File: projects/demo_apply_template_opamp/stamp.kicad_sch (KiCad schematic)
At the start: 3 parts, among them U1 LM358

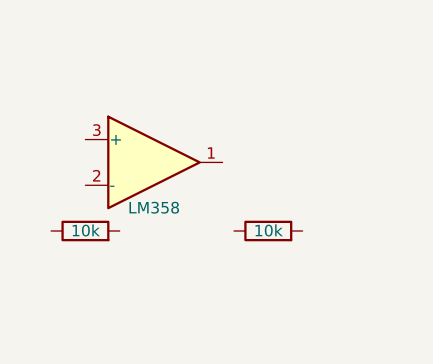
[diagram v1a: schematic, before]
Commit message: Phase 2: baked template geometry + LM358 embed fix
Templates now carry hand-authored wires/junctions/labels in relative
coords; Stamp() emits them verbatim. All 5 templates rewritten with
human conventions and self-verifying tests (gate.Check==0, TraceNets
contract, exact pin-endpoint match). flattenRawSymbol now inherits
parent properties so embedded derived symbols match KiCad 10
regeneration (fixes lib_symbol_mismatch for LM358/NE5532).

Co-Authored-By: Claude Fable 5 <noreply@anthropic.com>
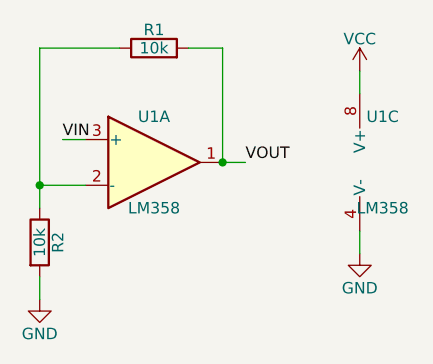
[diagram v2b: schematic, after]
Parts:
- added unit 3 of U1
- R1, R2, U1: now in the parts list
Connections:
- net at R1.1: now also R2.1, U1.2 (-)
- net VOUT: now reaches R1.2
- net VOUT: now also U1.1
- net VIN: now reaches U1.3 (+)
- net GND: now reaches R2.2
- net GND: now also U1.4 (V-)
- new net VCC: U1.8 (V+)
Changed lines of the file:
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@@
     (path "/" (page "1")))
   (symbol (lib_id "Amplifier_Operational:LM358")
-    (at 80.01 80.01 0) (unit 1) (exclude_from_sim no) (in_bom no) (on_board no) (dnp no)
+    (at 80.01 80.01 0) (unit 1) (exclude_from_sim no) (in_bom yes) (on_board yes) (dnp no)
     (property "Reference" "U1"
-      (at 80.01 80.01 0)
-      (effects
-        (font (size 1.27 1.27)) (hide yes)))
+      (at 80.01 74.93 0)
+      (effects
+        (font (size 1.27 1.27))))
     (property "Value" "LM358"
       (at 80.01 85.09 0)
@@
     (instances
       (project ""
-        (path "/e5270886-c330-482a-858b-eb20bea9dc9a" (reference "U1") (unit 1)))))
+        (path "/ca349aeb-c2b5-433f-8e31-d97ef754470a" (reference "U1") (unit 1)))))
+  (symbol (lib_id "Amplifier_Operational:LM358")
+    (at 105.41 80.01 0) (unit 3) (exclude_from_sim no) (in_bom yes) (on_board yes) (dnp no)
+    (property "Reference" "U1"
+      (at 105.41 74.93 0)
+      (effects
+        (font (size 1.27 1.27))))
+    (property "Value" "LM358"
+      (at 105.41 85.09 0)
+      (effects
+        (font (size 1.27 1.27))))
+    (property "Footprint" ""
+      (at 105.41 80.01 0)
+      (effects
+        (font (size 1.27 1.27)) (hide yes)))
+    (property "Datasheet" ""
+      (at 105.41 80.01 0)
+      (effects
+        (font (size 1.27 1.27)) (hide yes)))
+    (property "Description" ""
+      (at 105.41 80.01 0)
+      (effects
+        (font (size 1.27 1.27)) (hide yes)))
+    (pin "4")
+    (pin "8")
+    (instances
+      (project ""
+        (path "/ca349aeb-c2b5-433f-8e31-d97ef754470a" (reference "U1") (unit 3)))))
   (symbol (lib_id "Device:R")
-    (at 92.71 87.63 90) (unit 1) (exclude_from_sim no) (in_bom no) (on_board no) (dnp no)
+    (at 80.01 67.31 90) (unit 1) (exclude_from_sim no) (in_bom yes) (on_board yes) (dnp no)
     (property "Reference" "R1"
-      (at 92.71 87.63 0)
-      (effects
-        (font (size 1.27 1.27)) (hide yes)))
+      (at 80.01 65.278 90)
+      (effects
+        (font (size 1.27 1.27))))
     (property "Value" "10k"
-      (at 92.71 87.63 90)
-      (effects
-        (font (size 1.27 1.27))))
-    (property "Footprint" ""
-      (at 92.71 87.63 0)
-      (effects
-        (font (size 1.27 1.27)) (hide yes)))
-    (property "Datasheet" ""
-      (at 92.71 87.63 0)
-      (effects
-        (font (size 1.27 1.27)) (hide yes)))
-    (property "Description" ""
-      (at 92.71 87.63 0)
+      (at 80.01 67.31 90)
+      (effects
+        (font (size 1.27 1.27))))
+    (property "Footprint" ""
+      (at 80.01 67.31 0)
+      (effects
+        (font (size 1.27 1.27)) (hide yes)))
+    (property "Datasheet" ""
+      (at 80.01 67.31 0)
+      (effects
+        (font (size 1.27 1.27)) (hide yes)))
+    (property "Description" ""
+      (at 80.01 67.31 0)
       (effects
         (font (size 1.27 1.27)) (hide yes)))
@@
     (instances
       (project ""
-        (path "/e5270886-c330-482a-858b-eb20bea9dc9a" (reference "R1") (unit 1)))))
+        (path "/ca349aeb-c2b5-433f-8e31-d97ef754470a" (reference "R1") (unit 1)))))
   (symbol (lib_id "Device:R")
-    (at 72.39 87.63 90) (unit 1) (exclude_from_sim no) (in_bom no) (on_board no) (dnp no)
+    (at 67.31 88.9 0) (unit 1) (exclude_from_sim no) (in_bom yes) (on_board yes) (dnp no)
     (property "Reference" "R2"
-      (at 72.39 87.63 0)
-      (effects
-        (font (size 1.27 1.27)) (hide yes)))
+      (at 69.342 88.9 90)
+      (effects
+        (font (size 1.27 1.27))))
     (property "Value" "10k"
-      (at 72.39 87.63 90)
-      (effects
-        (font (size 1.27 1.27))))
-    (property "Footprint" ""
-      (at 72.39 87.63 0)
-      (effects
-        (font (size 1.27 1.27)) (hide yes)))
-    (property "Datasheet" ""
-      (at 72.39 87.63 0)
-      (effects
-        (font (size 1.27 1.27)) (hide yes)))
-    (property "Description" ""
-      (at 72.39 87.63 0)
+      (at 67.31 88.9 90)
+      (effects
+        (font (size 1.27 1.27))))
+    (property "Footprint" ""
+      (at 67.31 88.9 0)
+      (effects
+        (font (size 1.27 1.27)) (hide yes)))
+    (property "Datasheet" ""
+      (at 67.31 88.9 0)
+      (effects
+        (font (size 1.27 1.27)) (hide yes)))
+    (property "Description" ""
+      (at 67.31 88.9 0)
       (effects
         (font (size 1.27 1.27)) (hide yes)))
@@
     (instances
       (project ""
-        (path "/e5270886-c330-482a-858b-eb20bea9dc9a" (reference "R2") (unit 1))))))
+        (path "/ca349aeb-c2b5-433f-8e31-d97ef754470a" (reference "R2") (unit 1)))))
+  (symbol (lib_id "power:VCC")
+    (at 102.87 69.85 0) (unit 1) (exclude_from_sim no) (in_bom no) (on_board no) (dnp no)
+    (property "Reference" "#PWR1"
+      (at 102.87 69.85 0)
+      (effects
+        (font (size 1.27 1.27)) (hide yes)))
+    (property "Value" "VCC"
+      (at 102.87 66.294 0)
+      (effects
+        (font (size 1.27 1.27))))
+    (property "Footprint" ""
+      (at 102.87 69.85 0)
+      (effects
+        (font (size 1.27 1.27)) (hide yes)))
+    (property "Datasheet" ""
+      (at 102.87 69.85 0)
+      (effects
+        (font (size 1.27 1.27)) (hide yes)))
+    (property "Description" ""
+      (at 102.87 69.85 0)
+      (effects
+        (font (size 1.27 1.27)) (hide yes)))
+    (pin "1")
+    (instances
+      (project ""
+        (path "/ca349aeb-c2b5-433f-8e31-d97ef754470a" (reference "#PWR1") (unit 1)))))
+  (symbol (lib_id "power:GND")
+    (at 102.87 90.17 0) (unit 1) (exclude_from_sim no) (in_bom no) (on_board no) (dnp no)
+    (property "Reference" "#PWR2"
+      (at 102.87 90.17 0)
+      (effects
+        (font (size 1.27 1.27)) (hide yes)))
+    (property "Value" "GND"
+      (at 102.87 93.98 0)
+      (effects
+        (font (size 1.27 1.27))))
+    (property "Footprint" ""
+      (at 102.87 90.17 0)
+      (effects
+        (font (size 1.27 1.27)) (hide yes)))
+    (property "Datasheet" ""
+      (at 102.87 90.17 0)
+      (effects
+        (font (size 1.27 1.27)) (hide yes)))
+    (property "Description" ""
+      (at 102.87 90.17 0)
+      (effects
+        (font (size 1.27 1.27)) (hide yes)))
+    (pin "1")
+    (instances
+      (project ""
+        (path "/ca349aeb-c2b5-433f-8e31-d97ef754470a" (reference "#PWR2") (unit 1)))))
+  (symbol (lib_id "power:GND")
+    (at 67.31 95.25 0) (unit 1) (exclude_from_sim no) (in_bom no) (on_board no) (dnp no)
+    (property "Reference" "#PWR3"
+      (at 67.31 95.25 0)
+      (effects
+        (font (size 1.27 1.27)) (hide yes)))
+    (property "Value" "GND"
+      (at 67.31 99.06 0)
+      (effects
+        (font (size 1.27 1.27))))
+    (property "Footprint" ""
+      (at 67.31 95.25 0)
+      (effects
+        (font (size 1.27 1.27)) (hide yes)))
+    (property "Datasheet" ""
+      (at 67.31 95.25 0)
+      (effects
+        (font (size 1.27 1.27)) (hide yes)))
+    (property "Description" ""
+      (at 67.31 95.25 0)
+      (effects
+        (font (size 1.27 1.27)) (hide yes)))
+    (pin "1")
+    (instances
+      (project ""
+        (path "/ca349aeb-c2b5-433f-8e31-d97ef754470a" (reference "#PWR3") (unit 1)))))
+  (wire
+    (pts (xy 87.63 80.01) (xy 87.63 67.31))
+    (stroke (width 0) (type default)))
+  (wire
+    (pts (xy 87.63 67.31) (xy 83.82 67.31))
+    (stroke (width 0) (type default)))
+  (wire
+    (pts (xy 76.2 67.31) (xy 67.31 67.31))
+    (stroke (width 0) (type default)))
+  (wire
+    (pts (xy 67.31 67.31) (xy 67.31 82.55))
+    (stroke (width 0) (type default)))
+  (wire
+    (pts (xy 67.31 82.55) (xy 72.39 82.55))
+    (stroke (width 0) (type default)))
+  (wire
+    (pts (xy 67.31 82.55) (xy 67.31 85.09))
+    (stroke (width 0) (type default)))
+  (wire
+    (pts (xy 67.31 92.71) (xy 67.31 95.25))
+    (stroke (width 0) (type default)))
+  (wire
+    (pts (xy 87.63 80.01) (xy 90.17 80.01))
+    (stroke (width 0) (type default)))
+  (wire
+    (pts (xy 72.39 77.47) (xy 69.85 77.47))
+    (stroke (width 0) (type default)))
+  (wire
+    (pts (xy 102.87 72.39) (xy 102.87 69.85))
+    (stroke (width 0) (type default)))
+  (wire
+    (pts (xy 102.87 87.63) (xy 102.87 90.17))
+    (stroke (width 0) (type default)))
+  (junction (at 87.63 80.01) (diameter 0)
+    (color 0 0 0 0))
+  (junction (at 67.31 82.55) (diameter 0)
+    (color 0 0 0 0))
+  (label "VOUT"
+    (at 90.17 80.01 0) (fields_autoplaced yes)
+    (effects
+      (font (size 1.27 1.27)) (justify left bottom))
+    (property "Intersheet References" ""
+      (at 0 0 0)
+      (effects
+        (font (size 1.27 1.27)) (hide yes))))
+  (label "VIN"
+    (at 69.85 77.47 180) (fields_autoplaced yes)
+    (effects
+      (font (size 1.27 1.27)) (justify left bottom))
+    (property "Intersheet References" ""
+      (at 0 0 0)
+      (effects
+        (font (size 1.27 1.27)) (hide yes)))))
